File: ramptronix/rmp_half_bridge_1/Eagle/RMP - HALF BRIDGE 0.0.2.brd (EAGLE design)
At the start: 69 x 55.4 mm, 66 parts

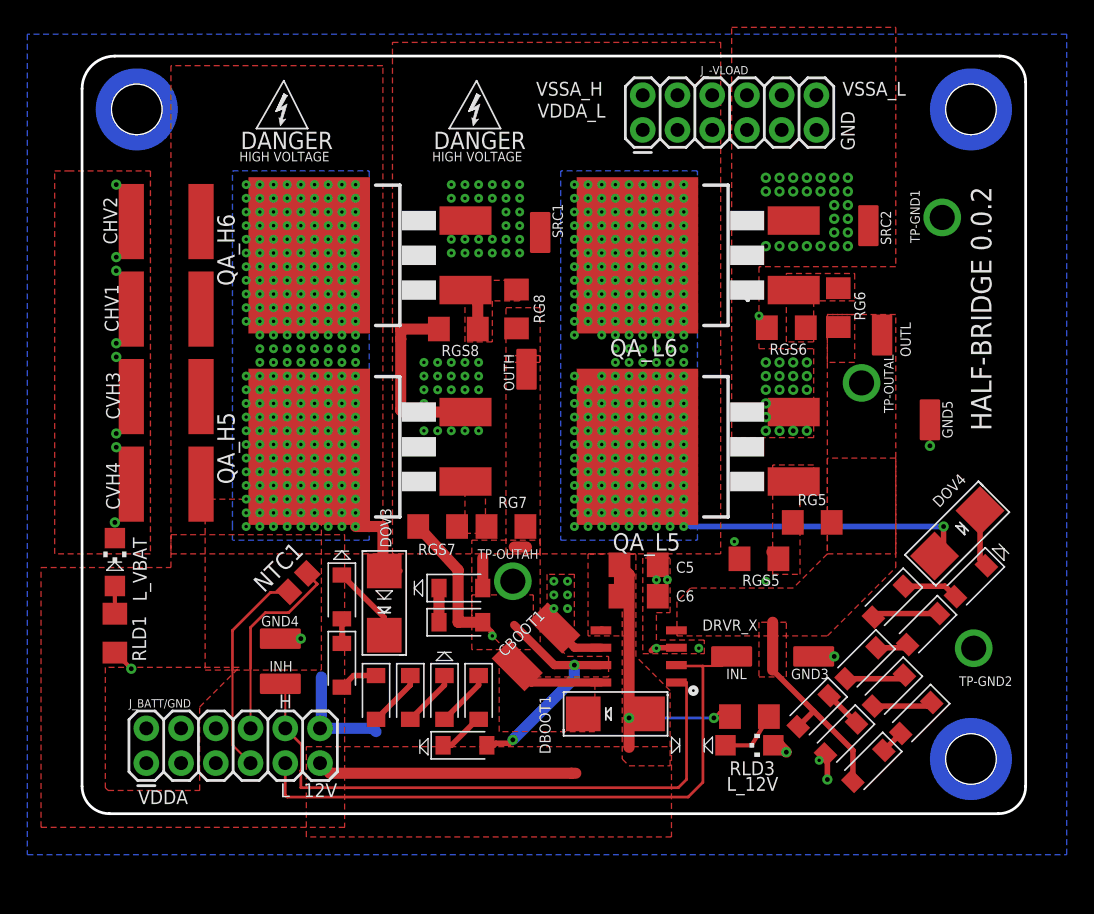
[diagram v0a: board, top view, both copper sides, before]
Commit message: Half Bridge - 0.0.2
Half Bridge - 0.0.2
Fixed net issue with OV clamp/crowbar
Increased voltage rating of MOSFETs
Increased voltage rating of CAPS
Increased clearances for 400V operation
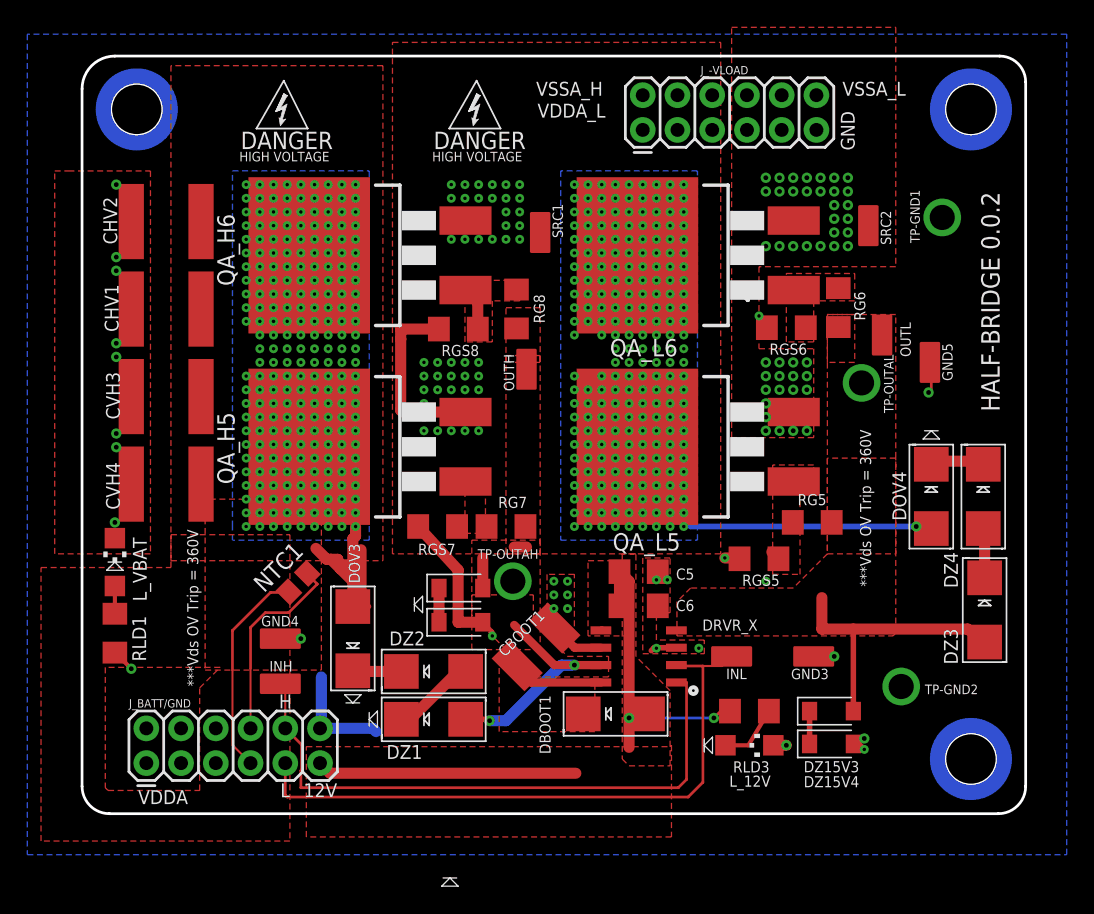
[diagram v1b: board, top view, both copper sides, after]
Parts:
- removed DZ24V1, DZ24V10, DZ24V11, DZ24V12, DZ24V17, DZ24V18, DZ24V19, DZ24V2, DZ24V22, DZ24V23, DZ24V24, DZ24V3, DZ24V4, DZ24V9: NZH15B,115, Diode:SODFL3718X115
- added DZ1, DZ2, DZ3, DZ4: (no value), adafruit:SMADIODE
- moved TP-GND2 5.99 mm to (59.9, 9.30)
- moved GND5 4.20 mm to (62.0, 33.0)
- moved DOV3 3.47 mm to (19.8, 12.8)
- moved DOV4 3.30 mm to (62.1, 23.2), turned to 270 degrees
- moved DZ15V3 1.30 mm to (54.8, 7.50), turned to 0 degrees
- moved DZ15V4 0.81 mm to (54.8, 5.10), turned to 0 degrees
- moved C6 0.70 mm to (40.7, 15.2)
- moved C5 0.50 mm to (40.7, 17.7)
- moved RLD3 0.40 mm to (48.8, 7.50)
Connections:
- removed net N$25: DZ24V10.1, DZ24V11.2
- removed net N$26: DZ24V11.1, DZ24V12.2
- removed net N$33: DZ24V10.2, DZ24V9.1
- removed net N$34: DZ24V17.1, DZ24V18.2
- removed net N$35: DZ24V18.1, DZ24V19.2
- removed net N$36: DOV4.C, DZ24V19.1
- removed net N$4: DZ24V22.2, DZ24V4.1
- removed net N$40: DZ24V22.1, DZ24V23.2
- removed net N$42: DZ24V23.1, DZ24V24.2
- removed net N$5: DZ24V12.1, DZ24V17.2
- net N$1: now also DZ1.C, DZ2.A; no longer DZ24V2.1, DZ24V3.2
- net N$2: now also DOV4.C, DZ4.C; no longer DZ24V3.1, DZ24V4.2
- net N$3: now also DZ3.C, DZ4.A; no longer DZ24V1.1, DZ24V2.2
- net N$47: now also DZ2.C; no longer DZ24V24.1
- net OUTA_H: now also DZ1.A; no longer DZ24V1.2
- net OUTA_L: now also DZ3.A; no longer DZ24V9.2
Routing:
- net VDDA: track 15.4 -> 26.4 mm
- net N$34: track 4.87 -> 0.00 mm
- net OUTA_L: track 15.7 -> 20.5 mm
- net N$26: track 4.37 -> 0.00 mm
- net N$25: track 4.37 -> 0.00 mm
- net VSS_A: track 59.1 -> 63.4 mm, vias 284 -> 278
- net N$4: track 4.24 -> 0.00 mm
- net N$36: track 4.22 -> 0.00 mm
- net N$35: track 4.05 -> 0.00 mm
- net N$40: track 2.85 -> 0.00 mm
- net N$5: track 2.33 -> 0.00 mm
- net N$47: track 5.68 -> 3.65 mm
- net N$33: track 1.99 -> 0.00 mm
- net N$1: track 4.24 -> 6.15 mm
- net N$42: track 1.80 -> 0.00 mm
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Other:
- board text added: "***Vds OV Trip = 360V"
